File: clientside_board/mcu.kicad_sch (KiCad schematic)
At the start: 9 parts, among them J1 Programming Connector, U1 PIC24EP512GU810-I/PT

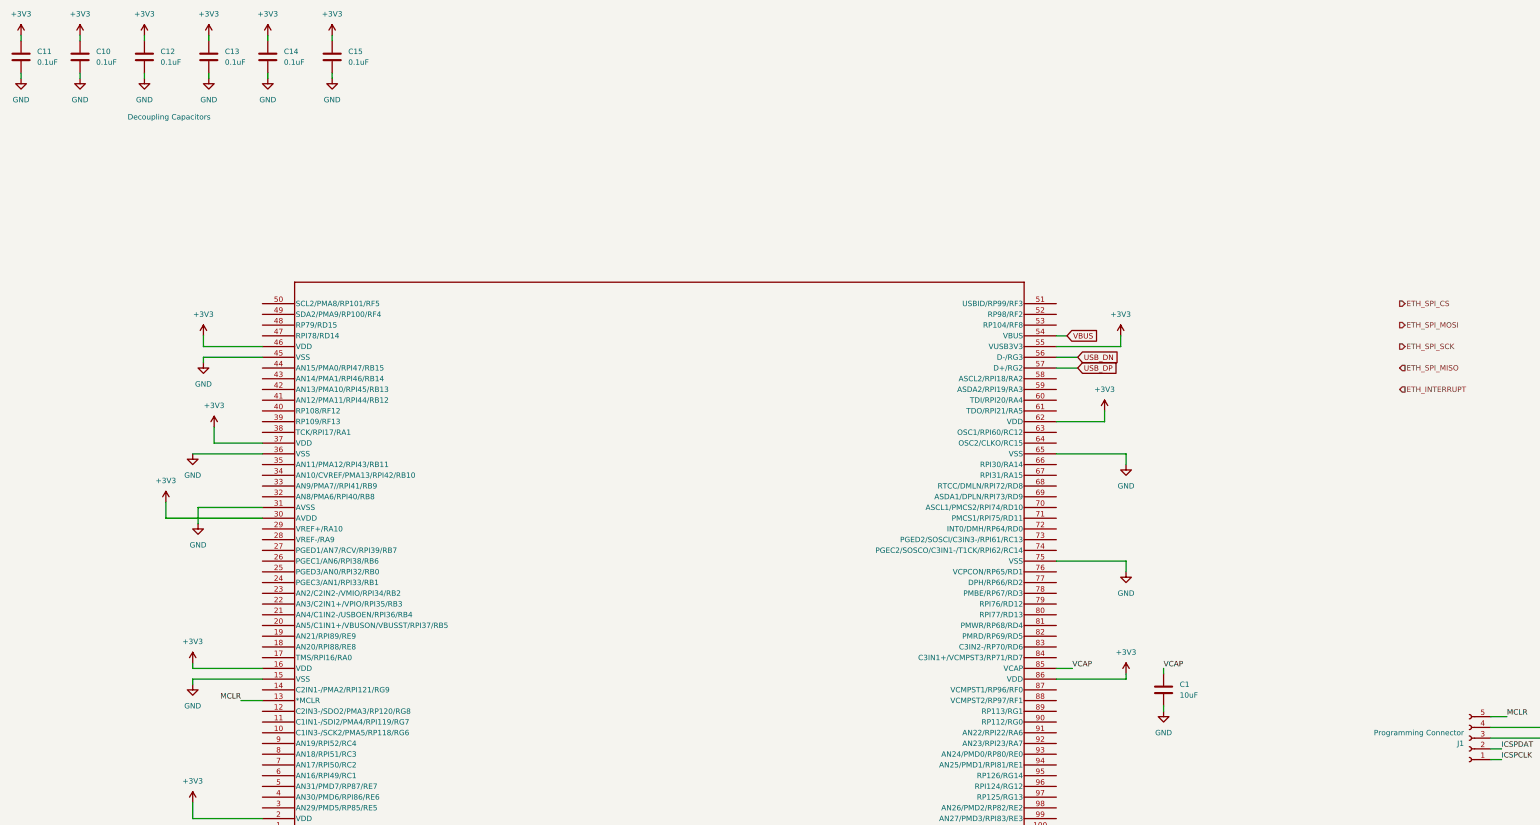
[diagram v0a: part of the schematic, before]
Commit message: Cleanup Power and Ethernet Sheet
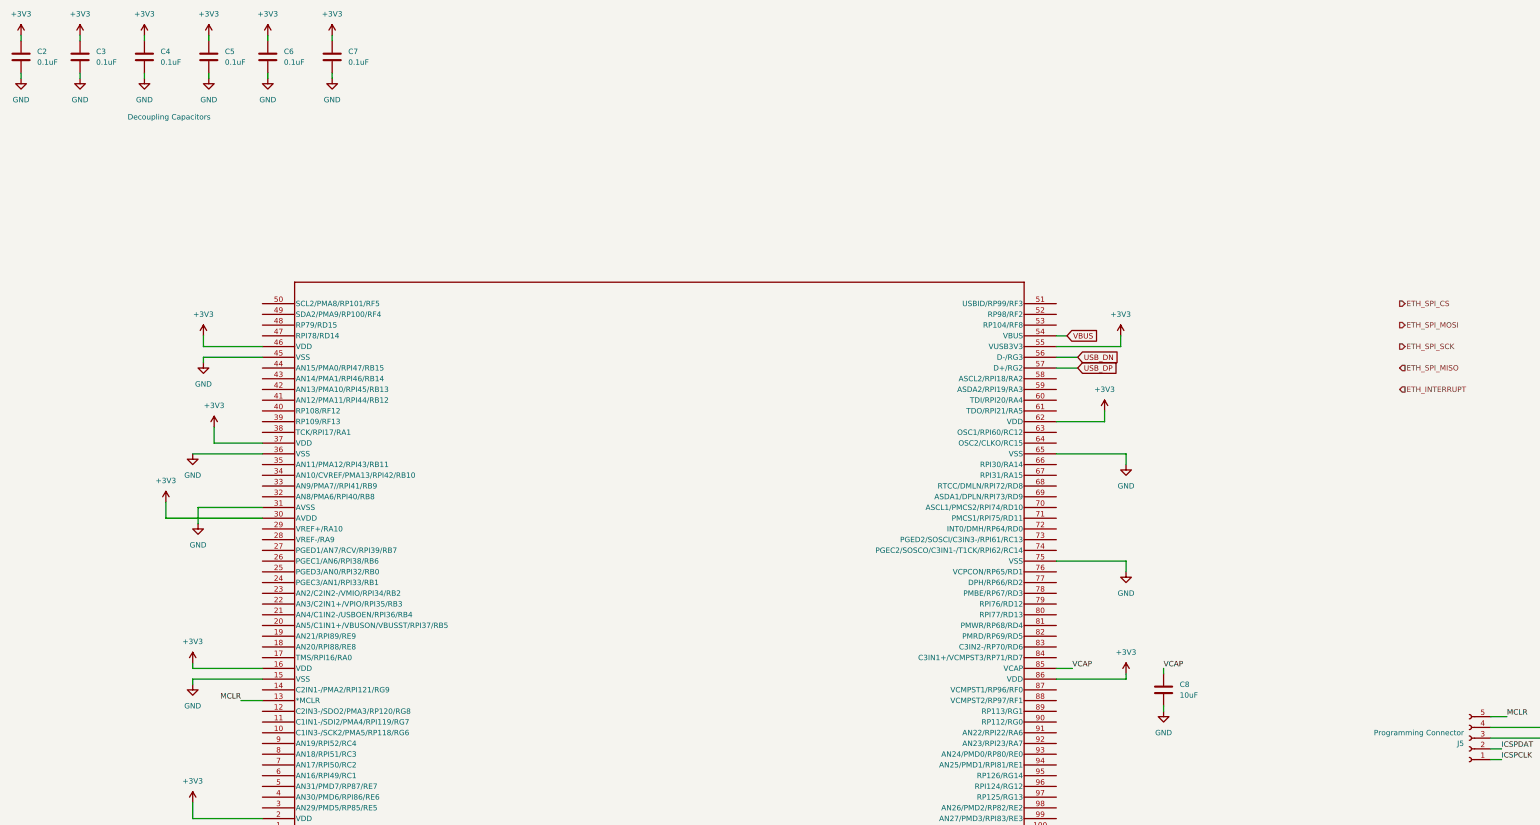
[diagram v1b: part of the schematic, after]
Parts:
- C2: renamed from C11; footprint (none) -> Capacitor_SMD:C_0805_2012Metric_Pad1.18x1.45mm_HandSolder
- C3: renamed from C10; footprint (none) -> Capacitor_SMD:C_0805_2012Metric_Pad1.18x1.45mm_HandSolder
- C4: renamed from C12; footprint (none) -> Capacitor_SMD:C_0805_2012Metric_Pad1.18x1.45mm_HandSolder
- C5: renamed from C13; footprint (none) -> Capacitor_SMD:C_0805_2012Metric_Pad1.18x1.45mm_HandSolder
- C6: renamed from C14; footprint (none) -> Capacitor_SMD:C_0805_2012Metric_Pad1.18x1.45mm_HandSolder
- C7: renamed from C15; footprint (none) -> Capacitor_SMD:C_0805_2012Metric_Pad1.18x1.45mm_HandSolder
- C8: renamed from C1; footprint (none) -> Capacitor_SMD:C_0805_2012Metric_Pad1.18x1.45mm_HandSolder
- renumbered J1 to J5

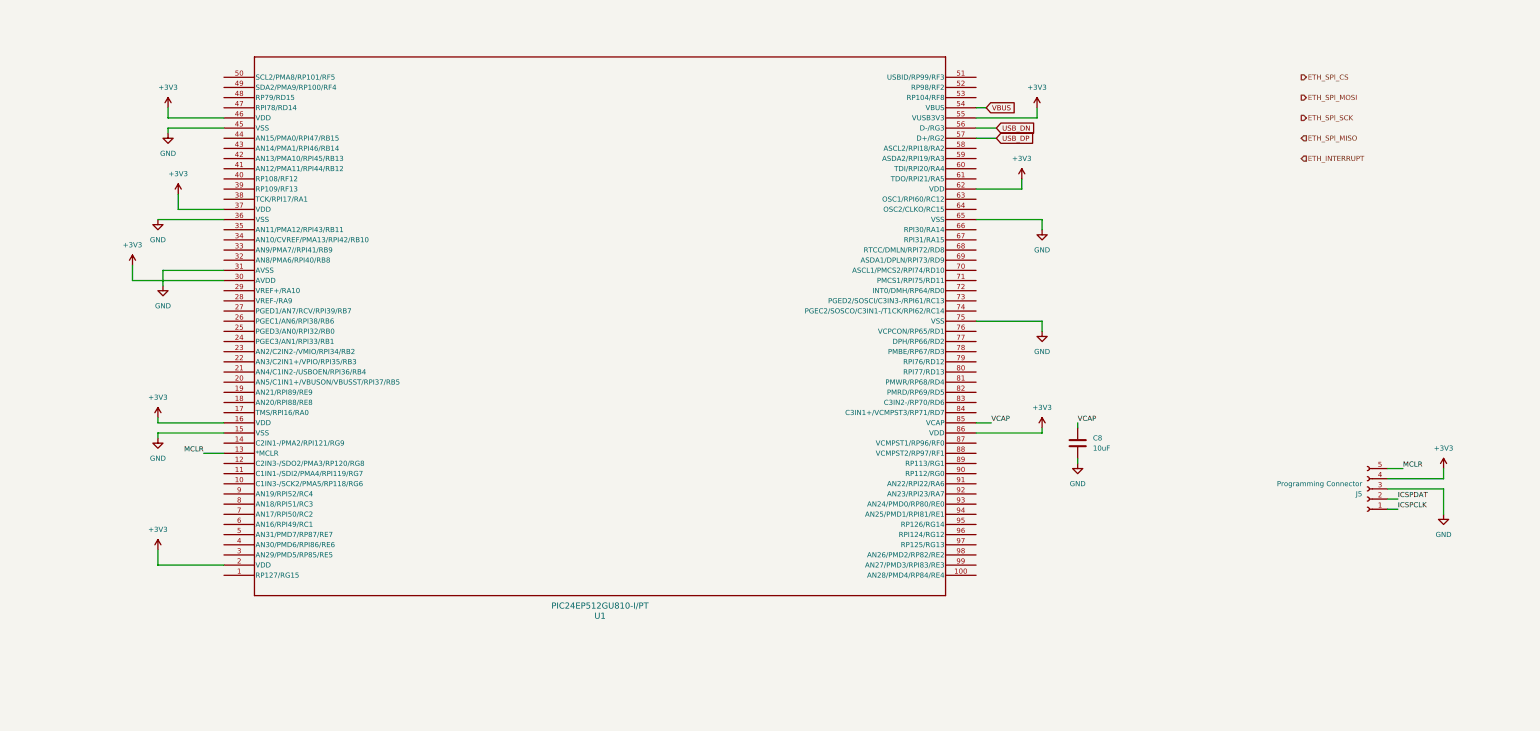
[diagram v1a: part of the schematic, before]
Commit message: Start MCU pin connection
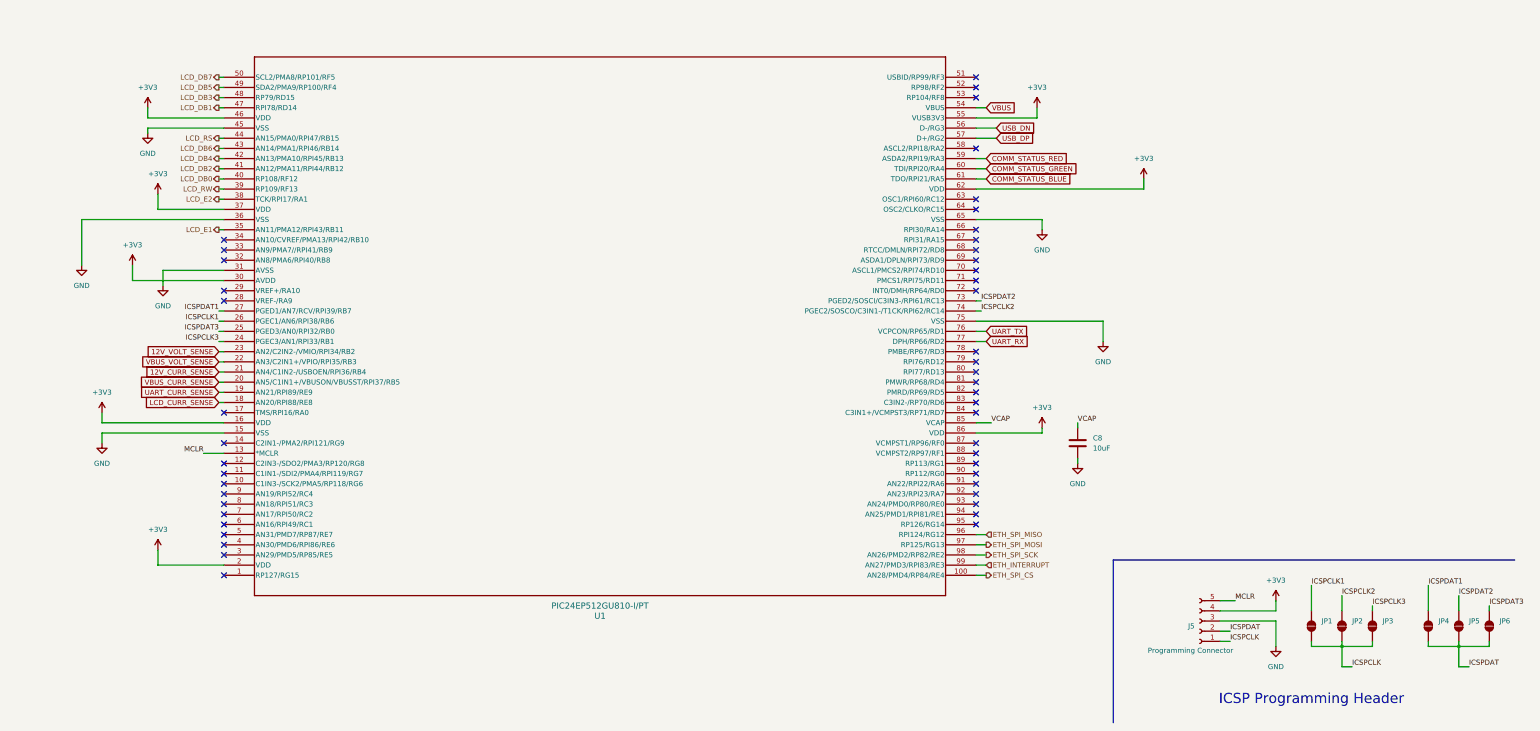
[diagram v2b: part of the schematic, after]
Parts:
- added JP1, JP2, JP3, JP4, JP5, JP6: SolderJumper_2_Open, symbol Jumper:SolderJumper_2_Open
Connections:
- net ETH_INTERRUPT: now also U1.99 (AN27/PMD3/RPI83/RE3)
- net ETH_SPI_CS: now also U1.100 (AN28/PMD4/RP84/RE4)
- net ETH_SPI_MISO: now also U1.96 (RPI124/RG12)
- net ETH_SPI_MOSI: now also U1.97 (RP125/RG13)
- net ETH_SPI_SCK: now also U1.98 (AN26/PMD2/RP82/RE2)
- net ICSPCLK: now also JP1.1 (A), JP2.1 (A), JP3.1 (A)
- net ICSPDAT: now also JP4.1 (A), JP5.1 (A), JP6.1 (A)
- net LCD_CURR_SENSE: now reaches U1.18 (AN20/RPI88/RE8)
- net UART_CURR_SENSE: now reaches U1.19 (AN21/RPI89/RE9)
- net VBUS_CURR_SENSE: now reaches U1.20 (AN5/C1IN1+/VBUSON/VBUSST/RPI37/RB5)
- net 12V_CURR_SENSE: now reaches U1.21 (AN4/C1IN2-/USBOEN/RPI36/RB4)
- net VBUS_VOLT_SENSE: now reaches U1.22 (AN3/C2IN1+/VPIO/RPI35/RB3)
- net 12V_VOLT_SENSE: now reaches U1.23 (AN2/C2IN2-/VMIO/RPI34/RB2)
- net ICSPCLK3: now reaches U1.24 (PGEC3/AN1/RPI33/RB1)
- net ICSPCLK3: now also JP3.2 (B)
- net ICSPDAT3: now reaches U1.25 (PGED3/AN0/RPI32/RB0)
- net ICSPDAT3: now also JP6.2 (B)
- net ICSPCLK1: now reaches U1.26 (PGEC1/AN6/RPI38/RB6)
- net ICSPCLK1: now also JP1.2 (B)
- net ICSPDAT1: now reaches U1.27 (PGED1/AN7/RCV/RPI39/RB7)
- net ICSPDAT1: now also JP4.2 (B)
- net LCD_E1: now reaches U1.35 (AN11/PMA12/RPI43/RB11)
- net LCD_E2: now reaches U1.38 (TCK/RPI17/RA1)
- net LCD_RW: now reaches U1.39 (RP109/RF13)
- net LCD_DB0: now reaches U1.40 (RP108/RF12)
- net LCD_DB2: now reaches U1.41 (AN12/PMA11/RPI44/RB12)
- net LCD_DB4: now reaches U1.42 (AN13/PMA10/RPI45/RB13)
- net LCD_DB6: now reaches U1.43 (AN14/PMA1/RPI46/RB14)
- net LCD_RS: now reaches U1.44 (AN15/PMA0/RPI47/RB15)
- net LCD_DB1: now reaches U1.47 (RPI78/RD14)
- net LCD_DB3: now reaches U1.48 (RP79/RD15)
- net LCD_DB5: now reaches U1.49 (SDA2/PMA9/RP100/RF4)
- net LCD_DB7: now reaches U1.50 (SCL2/PMA8/RP101/RF5)
- net COMM_STATUS_RED: now reaches U1.59 (ASDA2/RPI19/RA3)
- net COMM_STATUS_GREEN: now reaches U1.60 (TDI/RPI20/RA4)
- net COMM_STATUS_BLUE: now reaches U1.61 (TDO/RPI21/RA5)
- net ICSPDAT2: now reaches U1.73 (PGED2/SOSCI/C3IN3-/RPI61/RC13)
- net ICSPDAT2: now also JP5.2 (B)
- net ICSPCLK2: now reaches U1.74 (PGEC2/SOSCO/C3IN1-/T1CK/RPI62/RC14)
- net ICSPCLK2: now also JP2.2 (B)
- net UART_TX: now reaches U1.76 (VCPCON/RP65/RD1)
- net UART_RX: now reaches U1.77 (DPH/RP66/RD2)
- no-connect marks 0 -> 47
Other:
- note added: "ICSP Programming Header"
- moved on the sheet: J5

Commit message: Top sheet update
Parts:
- C2, C3, C4, C5, C6, C7, C8: footprint Capacitor_SMD:C_0805_2012Metric_Pad1.18x1.45mm_HandSolder -> Capacitor_SMD:C_0603_1608Metric_Pad1.08x0.95mm_HandSolder
